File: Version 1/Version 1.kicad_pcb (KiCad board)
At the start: 2 copper layers, 43 parts, among them J1 Conn_01x05, Q1 IPP015N04NF2SAKMA1, Q2 IPP015N04NF2SAKMA1, Q3 IPP015N04NF2SAKMA1, Q4 IPP015N04NF2SAKMA1, Q5 IPP015N04NF2SAKMA1, Q6 IPP015N04NF2SAKMA1, U0 YAAJ_BlackPill_SWD_Breakout, U1 TPS62932, U2 TPS62932, U3 TPS62932

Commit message: updated schem
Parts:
- removed U0: YAAJ_BlackPill_SWD_Breakout, Footprints:YAAJ_BlackPill_SWD_1
- added C1: 470n, Capacitor_THT:C_Disc_D3.4mm_W2.1mm_P2.50mm, F.Cu at (178.0, 69.5)
- added C2: 470n, Capacitor_THT:C_Disc_D3.4mm_W2.1mm_P2.50mm, F.Cu at (178.0, 73.1)
- added C3: 470n, Capacitor_THT:C_Disc_D3.4mm_W2.1mm_P2.50mm, F.Cu at (178.0, 76.8)
- added C4: 47n, Capacitor_THT:C_Disc_D3.4mm_W2.1mm_P2.50mm, F.Cu at (178.0, 80.4)
- added C5: 2.2u, Capacitor_THT:CP_Radial_D5.0mm_P2.50mm, F.Cu at (178.7, 93.0)
- added C6: 47n, Capacitor_THT:C_Disc_D3.4mm_W2.1mm_P2.50mm, F.Cu at (178.0, 84.1)
- added C7: 2.2u, Capacitor_THT:CP_Radial_D5.0mm_P2.50mm, F.Cu at (178.7, 99.5)
- added C8: 47n, Capacitor_THT:C_Disc_D3.4mm_W2.1mm_P2.50mm, F.Cu at (178.0, 87.7)
- added C9: 2.2u, Capacitor_THT:CP_Radial_D5.0mm_P2.50mm, F.Cu at (178.7, 106.1)
- added L1: 10u, Inductor_THT:L_Axial_L13.0mm_D4.5mm_P7.62mm_Vertical_Fastron_HCCC, F.Cu at (139.7, 125.1)
- added L2: 15u, Inductor_THT:L_Axial_L13.0mm_D4.5mm_P7.62mm_Vertical_Fastron_HCCC, F.Cu at (139.7, 131.2)
- added L3: 7.8u, Inductor_THT:L_Axial_L13.0mm_D4.5mm_P7.62mm_Vertical_Fastron_HCCC, F.Cu at (139.7, 137.2)
- added R10: 10, Resistor_THT:R_Axial_DIN0207_L6.3mm_D2.5mm_P10.16mm_Horizontal, F.Cu at (151.6, 95.8)
- added R11: 4.7, Resistor_THT:R_Axial_DIN0207_L6.3mm_D2.5mm_P10.16mm_Horizontal, F.Cu at (151.6, 99.8)
- added R12: 4.7, Resistor_THT:R_Axial_DIN0207_L6.3mm_D2.5mm_P10.16mm_Horizontal, F.Cu at (151.6, 103.9)
- added R13: 10, Resistor_THT:R_Axial_DIN0207_L6.3mm_D2.5mm_P10.16mm_Horizontal, F.Cu at (151.6, 107.9)
- added R14: 4.7, Resistor_THT:R_Axial_DIN0207_L6.3mm_D2.5mm_P10.16mm_Horizontal, F.Cu at (151.6, 112.0)
- added R15: 4.7, Resistor_THT:R_Axial_DIN0207_L6.3mm_D2.5mm_P10.16mm_Horizontal, F.Cu at (151.6, 116.0)
- added R16: 10, Resistor_THT:R_Axial_DIN0207_L6.3mm_D2.5mm_P10.16mm_Horizontal, F.Cu at (151.6, 120.1)
- added R17: 4.7, Resistor_THT:R_Axial_DIN0207_L6.3mm_D2.5mm_P10.16mm_Horizontal, F.Cu at (164.9, 91.7)
- added R18: 4.7, Resistor_THT:R_Axial_DIN0207_L6.3mm_D2.5mm_P10.16mm_Horizontal, F.Cu at (164.9, 95.8)
- added R4: 10k, Resistor_THT:R_Axial_DIN0207_L6.3mm_D2.5mm_P10.16mm_Horizontal, F.Cu at (138.3, 103.9)
- added R5: 10k, Resistor_THT:R_Axial_DIN0207_L6.3mm_D2.5mm_P10.16mm_Horizontal, F.Cu at (138.3, 107.9)
- added R6: 10k, Resistor_THT:R_Axial_DIN0207_L6.3mm_D2.5mm_P10.16mm_Horizontal, F.Cu at (138.3, 112.0)
- added R7: 10k, Resistor_THT:R_Axial_DIN0207_L6.3mm_D2.5mm_P10.16mm_Horizontal, F.Cu at (138.3, 116.0)
- added R8: 10k, Resistor_THT:R_Axial_DIN0207_L6.3mm_D2.5mm_P10.16mm_Horizontal, F.Cu at (138.3, 120.1)
- added R9: 10k, Resistor_THT:R_Axial_DIN0207_L6.3mm_D2.5mm_P10.16mm_Horizontal, F.Cu at (151.6, 91.7)
- added U7: YAAJ_BlackPill_SWD_BreakoutV2, STM32:Blackpill, F.Cu at (123.1, 89.0)
- moved Q4 58.6 mm to (186.8, 112.3)
- moved Q1 58.6 mm to (186.8, 93.4)
- moved Q2 58.6 mm to (186.8, 99.7)
- moved Q3 58.6 mm to (186.8, 106.0)
- moved Q5 58.6 mm to (186.8, 118.6)
- moved Q6 58.6 mm to (186.8, 124.9)
- moved D1 56.1 mm to (159.9, 123.7)
- moved D4 50.1 mm to (159.9, 138.0)
- moved D2 50.1 mm to (159.9, 130.9)
- moved D3 50.1 mm to (159.9, 134.4)
- moved J1 49.4 mm to (171.2, 130.8)
- moved R1 49.1 mm to (138.3, 91.7)
- moved R2 49.1 mm to (138.3, 95.8)
- moved R3 49.1 mm to (138.3, 99.8)
- moved Cout1 45.4 mm to (127.2, 96.7)
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
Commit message: updated circuit
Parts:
- added J_RPI1: Conn_01x04, Connector_JST:JST_ACH_BM04B-ACHSS-A-GAN-ETF_1x04-1MP_P1.20mm_Vertical, F.Cu at (26.2, 96.0)
- moved Q5 170.2 mm to (44.5, 25.4)
- moved Q6 170.2 mm to (44.5, 31.7)
- moved D4 159.0 mm to (30.5, 45.7)
- moved C8 156.8 mm to (36.1, 21.0)
- moved C9 156.8 mm to (36.8, 39.4)
- moved R17 156.8 mm to (23.0, 25.0)
- moved R18 156.8 mm to (23.0, 29.1)
- moved R16 155.1 mm to (21.6, 35.6)
- moved C1 146.7 mm to (41.9, 124.2)
- moved L3 142.7 mm to (249.3, 45.8)
- moved Cout3 142.7 mm to (236.8, 33.4)
- moved D1 141.9 mm to (29.2, 179.1)
- moved Jin1 141.9 mm to (23.2, 182.0)
- moved Jout1 141.9 mm to (23.2, 191.1)
- moved C2 132.3 mm to (71.2, 151.1)
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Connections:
- R4 pad 1: INL_U -> SD_U
- R5 pad 1: INH_U -> IN_U
- R6 pad 1: INH_V -> IN_V
- R7 pad 1: INL_V -> SD_V
- R8 pad 1: INH_W -> IN_W
- R9 pad 1: INL_W -> SD_W
- U7 pad 12: unconnected-(U7-A6-Pad12) -> IN_U
- U7 pad 13: unconnected-(U7-A7-Pad13) -> IN_V
- U7 pad 14: unconnected-(U7-B0-Pad14) -> IN_W
- U7 pad 17: unconnected-(U7-B10-Pad17) -> SCL_RPI
- U7 pad 2: HallU -> SD_U
- U7 pad 3: HallV -> SD_V
- U7 pad 31: unconnected-(U7-B3-Pad31) -> SDA_RPI
- U7 pad 33: unconnected-(U7-B5-Pad33) -> HallU
- U7 pad 34: unconnected-(U7-B6-Pad34) -> HallV
- U7 pad 35: unconnected-(U7-B7-Pad35) -> HallW
- U7 pad 4: HallW -> SD_W

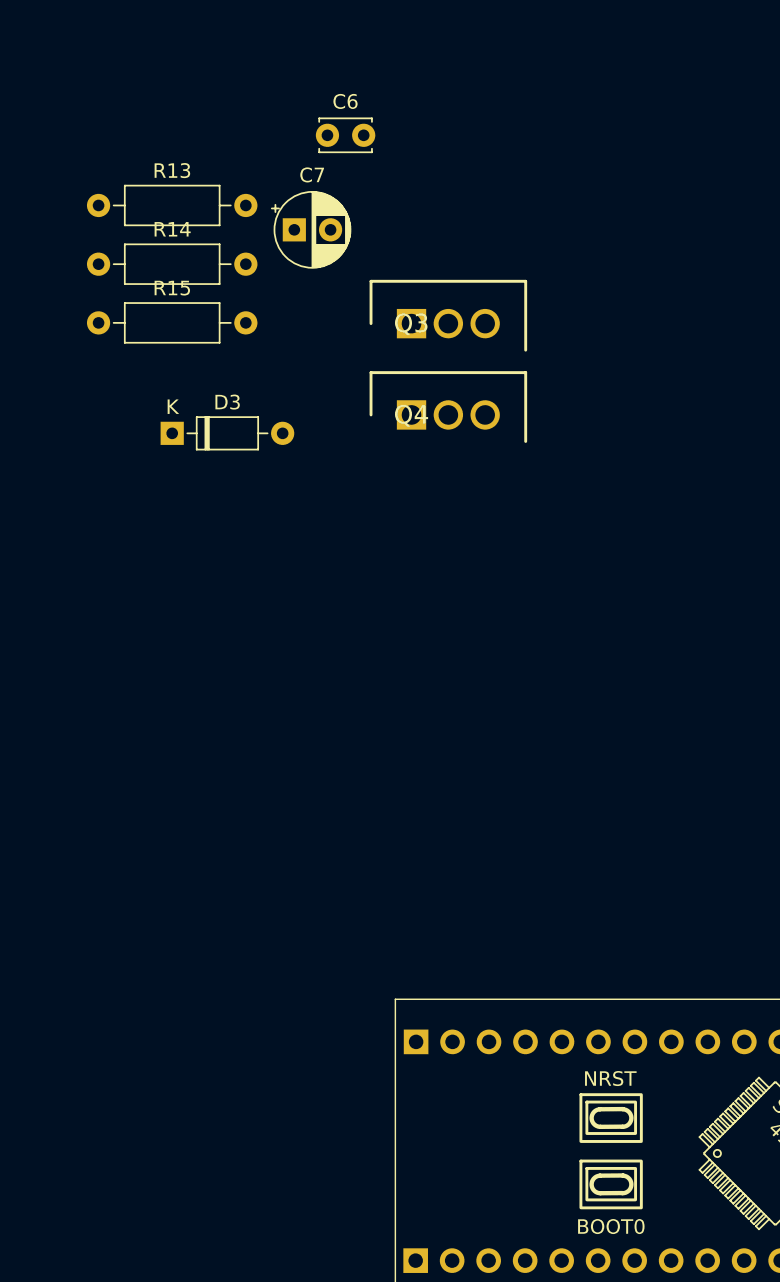
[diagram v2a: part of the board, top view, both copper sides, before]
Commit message: added 3D models
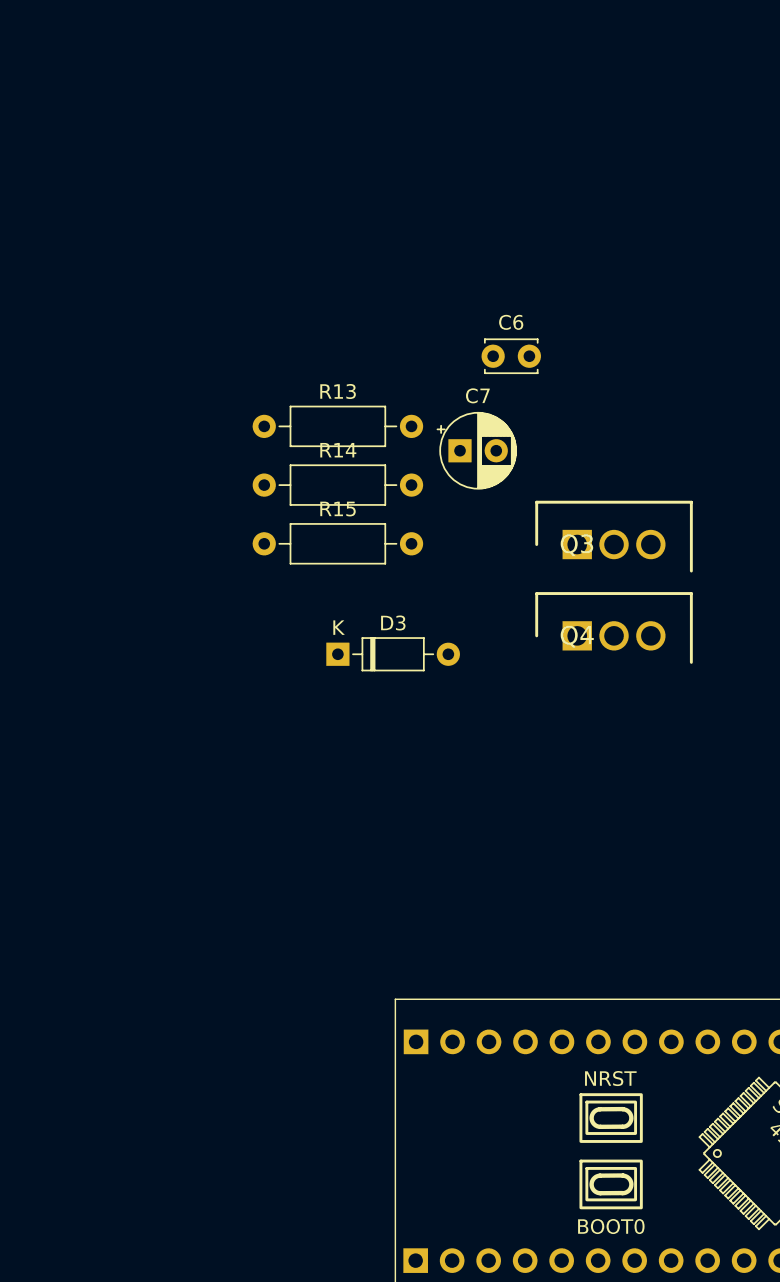
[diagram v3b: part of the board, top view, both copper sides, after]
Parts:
- moved Q4 19.1 mm to (125.7, 66.0)
- moved Q3 19.1 mm to (125.7, 59.7)
- moved R13 19.1 mm to (104.1, 51.6)
- moved R14 19.1 mm to (104.1, 55.6)
- moved R15 19.1 mm to (104.1, 59.7)
- moved C7 19.0 mm to (117.6, 53.3)
- moved D3 19.0 mm to (109.2, 67.3)
- moved C6 19.0 mm to (119.9, 46.8)
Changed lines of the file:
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@@
 		(fp_arc
 			(start 15.70391 -13.191849)
-			(mid 16.279999 -12.568861)
+			(mid 16.27999 -12.568861)
 			(end 15.669059 -11.98)
 			(stroke
@@
 		(fp_arc
 			(start 15.70391 -8.611849)
-			(mid 16.279999 -7.988861)
+			(mid 16.27999 -7.988861)
 			(end 15.669059 -7.4)
 			(stroke
@@
 			)
 		)
-		(model "D:/Users/admin/Documents/KiCad/Libraries/packages3d/Modules/STM32_Black_Pill/YAAJ_BlackPill_PinHeaders_B_SWD_cp.wrl"
+		(model "C:/Users/lauwy/RSP-CLOUD/School/Jaar 3/PROJ4/Schem/Custom SYmbol/Black Pill.step"
+			(hide yes)
 			(offset
-				(xyz 0 0 0)
+				(xyz 25.4 10.4 4.5)
 			)
 			(scale
@@
 			)
 		)
-		(model "D:/Users/admin/Documents/KiCad/Libraries/packages3d/Modules/STM32_Black_Pill/YAAJ_BlackPill_PinSockets_B_SWD_cp.wrl"
+		(model "C:/Users/lauwy/RSP-CLOUD/School/Jaar 3/PROJ4/Schem/Custom SYmbol/3dexport_balckpill_f401_v10_step_1656786165/BalckPill_F401 v31.step"
 			(offset
-				(xyz 0 0 0)
+				(xyz 0 0 3)
 			)
 			(scale
@@
 			)
 			(rotate
-				(xyz 0 0 0)
+				(xyz -90 0 0)
 			)
 		)
@@
 			)
 		)
+		(model "C:/Users/lauwy/RSP-CLOUD/School/Jaar 3/PROJ4/Schem/Custom SYmbol/MP2182GTL-Z--3DModel-STEP-56544.STEP"
+			(offset
+				(xyz 0 0 0)
+			)
+			(scale
+				(xyz 1 1 1)
+			)
+			(rotate
+				(xyz -90 0 90)
+			)
+		)
 	)
 	(footprint "Inductor_THT:L_Axial_L13.0mm_D4.5mm_P7.62mm_Vertical_Fastron_HCCC"
@@
 			)
 		)
+		(model "C:/Users/lauwy/RSP-CLOUD/School/Jaar 3/PROJ4/Schem/Custom SYmbol/MP2182GTL-Z--3DModel-STEP-56544.STEP"
+			(offset
+				(xyz 0 0 0)
+			)
+			(scale
+				(xyz 1 1 1)
+			)
+			(rotate
+				(xyz -90 0 90)
+			)
+		)
 	)
 	(footprint "Capacitor_THT:CP_Radial_D5.0mm_P2.50mm"
@@
 			)
 		)
+		(model "C:/Users/lauwy/RSP-CLOUD/School/Jaar 3/PROJ4/Schem/Custom SYmbol/MP2182GTL-Z--3DModel-STEP-56544.STEP"
+			(offset
+				(xyz 0 0 0)
+			)
+			(scale
+				(xyz 1 1 1)
+			)
+			(rotate
+				(xyz -90 0 90)
+			)
+		)
 	)
 	(footprint "Diode_THT:D_DO-35_SOD27_P7.62mm_Horizontal"
 		(layer "F.Cu")
-		(at 97.79 52.07)
+		(at 109.22 67.31)
 		(descr "Diode, DO-35_SOD27 series, Axial, Horizontal, pin pitch=7.62mm, , length*diameter=4*2mm^2, , http://www.diodes.com/_files/packages/DO-35.pdf")
 		(tags "Diode DO-35_SOD27 series Axial Horizontal pin pitch 7.62mm  length 4mm diameter 2mm")
@@
 	(footprint "Resistor_THT:R_Axial_DIN0207_L6.3mm_D2.5mm_P10.16mm_Horizontal"
 		(layer "F.Cu")
-		(at 92.71 36.35)
+		(at 104.14 51.59)
 		(descr "Resistor, Axial_DIN0207 series, Axial, Horizontal, pin pitch=10.16mm, 0.25W = 1/4W, length*diameter=6.3*2.5mm^2, http://cdn-reichelt.de/documents/datenblatt/B400/1_4W%23YAG.pdf")
 		(tags "Resistor Axial_DIN0207 series Axial Horizontal pin pitch 10.16mm 0.25W = 1/4W length 6.3mm diameter 2.5mm")
@@
 	(footprint "Resistor_THT:R_Axial_DIN0207_L6.3mm_D2.5mm_P10.16mm_Horizontal"
 		(layer "F.Cu")
-		(at 92.71 40.4)
+		(at 104.14 55.64)
 		(descr "Resistor, Axial_DIN0207 series, Axial, Horizontal, pin pitch=10.16mm, 0.25W = 1/4W, length*diameter=6.3*2.5mm^2, http://cdn-reichelt.de/documents/datenblatt/B400/1_4W%23YAG.pdf")
 		(tags "Resistor Axial_DIN0207 series Axial Horizontal pin pitch 10.16mm 0.25W = 1/4W length 6.3mm diameter 2.5mm")
@@
 	(footprint "LIB_IPP015N04NF2SAKMA1:TO254P475X1028X1996-3P"
 		(layer "F.Cu")
-		(at 114.3 44.5)
+		(at 125.73 59.74)
 		(descr "PG-TO220-3-U05")
 		(tags "MOSFET (N-Channel)")
@@
 			)
 		)
+		(model "C:/Users/lauwy/RSP-CLOUD/School/Jaar 3/PROJ4/Schem/Custom SYmbol/TO-220-1.step"
+			(offset
+				(xyz 2.5 3.5 4.5)
+			)
+			(scale
+				(xyz 1 1 1)
+			)
+			(rotate
+				(xyz 0 0 0)
+			)
+		)
 	)
 	(footprint "Connector_JST:JST_ACH_BM04B-ACHSS-A-GAN-ETF_1x04-1MP_P1.20mm_Vertical"
@@
 	(footprint "Capacitor_THT:CP_Radial_D5.0mm_P2.50mm"
 		(layer "F.Cu")
-		(at 106.214775 38.03)
+		(at 117.644775 53.27)
 		(descr "CP, Radial series, Radial, pin pitch=2.50mm, , diameter=5mm, Electrolytic Capacitor")
 		(tags "CP Radial series Radial pin pitch 2.50mm  diameter 5mm Electrolytic Capacitor")
@@
 	(footprint "Resistor_THT:R_Axial_DIN0207_L6.3mm_D2.5mm_P10.16mm_Horizontal"
 		(layer "F.Cu")
-		(at 92.71 44.45)
+		(at 104.14 59.69)
 		(descr "Resistor, Axial_DIN0207 series, Axial, Horizontal, pin pitch=10.16mm, 0.25W = 1/4W, length*diameter=6.3*2.5mm^2, http://cdn-reichelt.de/documents/datenblatt/B400/1_4W%23YAG.pdf")
 		(tags "Resistor Axial_DIN0207 series Axial Horizontal pin pitch 10.16mm 0.25W = 1/4W length 6.3mm diameter 2.5mm")
@@
 	(footprint "Capacitor_THT:C_Disc_D3.4mm_W2.1mm_P2.50mm"
 		(layer "F.Cu")
-		(at 108.500225 31.51)
+		(at 119.930225 46.75)
 		(descr "C, Disc series, Radial, pin pitch=2.50mm, , diameter*width=3.4*2.1mm^2, Capacitor, http://www.vishay.com/docs/45233/krseries.pdf")
 		(tags "C Disc series Radial pin pitch 2.50mm  diameter 3.4mm width 2.1mm Capacitor")
@@
 			)
 		)
+		(model "C:/Users/lauwy/RSP-CLOUD/School/Jaar 3/PROJ4/Schem/Custom SYmbol/TO-220-1.step"
+			(offset
+				(xyz 2.5 3.5 4.5)
+			)
+			(scale
+				(xyz 1 1 1)
+			)
+			(rotate
+				(xyz 0 0 0)
+			)
+		)
 	)
 	(footprint "Resistor_THT:R_Axial_DIN0207_L6.3mm_D2.5mm_P10.16mm_Horizontal"
@@
 		(model "IPP015N04NF2SAKMA1.stp"
 			(offset
+				(xyz 2.5 3.5 4.5)
+			)
+			(scale
+				(xyz 1 1 1)
+			)
+			(rotate
 				(xyz 0 0 0)
 			)
+		)
+		(model "C:/Users/lauwy/RSP-CLOUD/School/Jaar 3/PROJ4/Schem/Custom SYmbol/TO-220-1.step"
+			(offset
+				(xyz 2.5 3.5 4.5)
+			)
 			(scale
 				(xyz 1 1 1)
@@
 	(footprint "LIB_IPP015N04NF2SAKMA1:TO254P475X1028X1996-3P"
 		(layer "F.Cu")
-		(at 114.3 50.8)
+		(at 125.73 66.04)
 		(descr "PG-TO220-3-U05")
 		(tags "MOSFET (N-Channel)")
@@
 			)
 		)
+		(model "C:/Users/lauwy/RSP-CLOUD/School/Jaar 3/PROJ4/Schem/Custom SYmbol/TO-220-1.step"
+			(offset
+				(xyz 2.5 3.5 4.5)
+			)
+			(scale
+				(xyz 1 1 1)
+			)
+			(rotate
+				(xyz 0 0 0)
+			)
+		)
 	)
 	(footprint "Capacitor_THT:C_Disc_D3.4mm_W2.1mm_P2.50mm"
@@
 			)
 		)
+		(model "C:/Users/lauwy/RSP-CLOUD/School/Jaar 3/PROJ4/Schem/Custom SYmbol/TO-220-1.step"
+			(offset
+				(xyz 2.5 3.5 4.5)
+			)
+			(scale
+				(xyz 1 1 1)
+			)
+			(rotate
+				(xyz 0 0 0)
+			)
+		)
 	)
 	(footprint "Capacitor_THT:CP_Radial_D5.0mm_P2.50mm"
@@
 		(model "IPP015N04NF2SAKMA1.stp"
 			(offset
+				(xyz 2.5 3.5 4.5)
+			)
+			(scale
+				(xyz 1 1 1)
+			)
+			(rotate
 				(xyz 0 0 0)
 			)
+		)
+		(model "C:/Users/lauwy/RSP-CLOUD/School/Jaar 3/PROJ4/Schem/Custom SYmbol/TO-220-1.step"
+			(offset
+				(xyz 2.5 3.5 4.5)
+			)
 			(scale

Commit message: latest 3d components
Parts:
- added U4: IRS2004, IRS2004PBF:DIP762W56P254L988H533Q8N, F.Cu at (158.8, 50.8)
- added U5: IRS2004, IRS2004PBF:DIP762W56P254L988H533Q8N, F.Cu at (121.9, 76.2)
- added U6: IRS2004, IRS2004PBF:DIP762W56P254L988H533Q8N, F.Cu at (53.3, 44.5)

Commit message: udpated pcb
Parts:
- added U8: Conn_01x01_Socket, MountingHole:MountingHole_4.3mm_M4_DIN965_Pad, F.Cu at (76.8, 111.0)
- added V1: Conn_01x01_Socket, MountingHole:MountingHole_4.3mm_M4_DIN965_Pad, F.Cu at (86.2, 111.0)
- added W1: Conn_01x01_Socket, MountingHole:MountingHole_4.3mm_M4_DIN965_Pad, F.Cu at (95.6, 111.0)
- moved J1 189.9 mm to (61.4, 94.5), turned to -90 degrees
- moved R2 188.8 mm to (55.1, 79.3), turned to -90 degrees
- moved Rfbb1 185.5 mm to (82.1, 63.0)
- moved R3 183.8 mm to (58.9, 79.3), turned to -90 degrees
- moved R1 178.8 mm to (62.7, 79.3), turned to -90 degrees
- moved Cin1 178.8 mm to (105.1, 65.6)
- moved Rfbt1 177.4 mm to (92.3, 66.8), turned to 180 degrees
- moved Rfbt3 177.0 mm to (82.4, 39.9)
- moved Q1 172.0 mm to (18.4, 19.9), turned to -90 degrees
- moved U1 172.0 mm to (100.4, 60.0), turned to 180 degrees
- moved Q2 171.1 mm to (18.4, 36.4), turned to -90 degrees
- moved Cin3 169.1 mm to (104.0, 38.7)
- moved Cff1 168.6 mm to (96.1, 66.8), turned to 90 degrees
- moved Cboot1 167.9 mm to (97.3, 54.1)
- moved Rfbb3 167.3 mm to (92.6, 36.1), turned to 180 degrees
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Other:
- board outline added: 97.2 x 106 mm
